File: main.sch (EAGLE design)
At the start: 12 parts

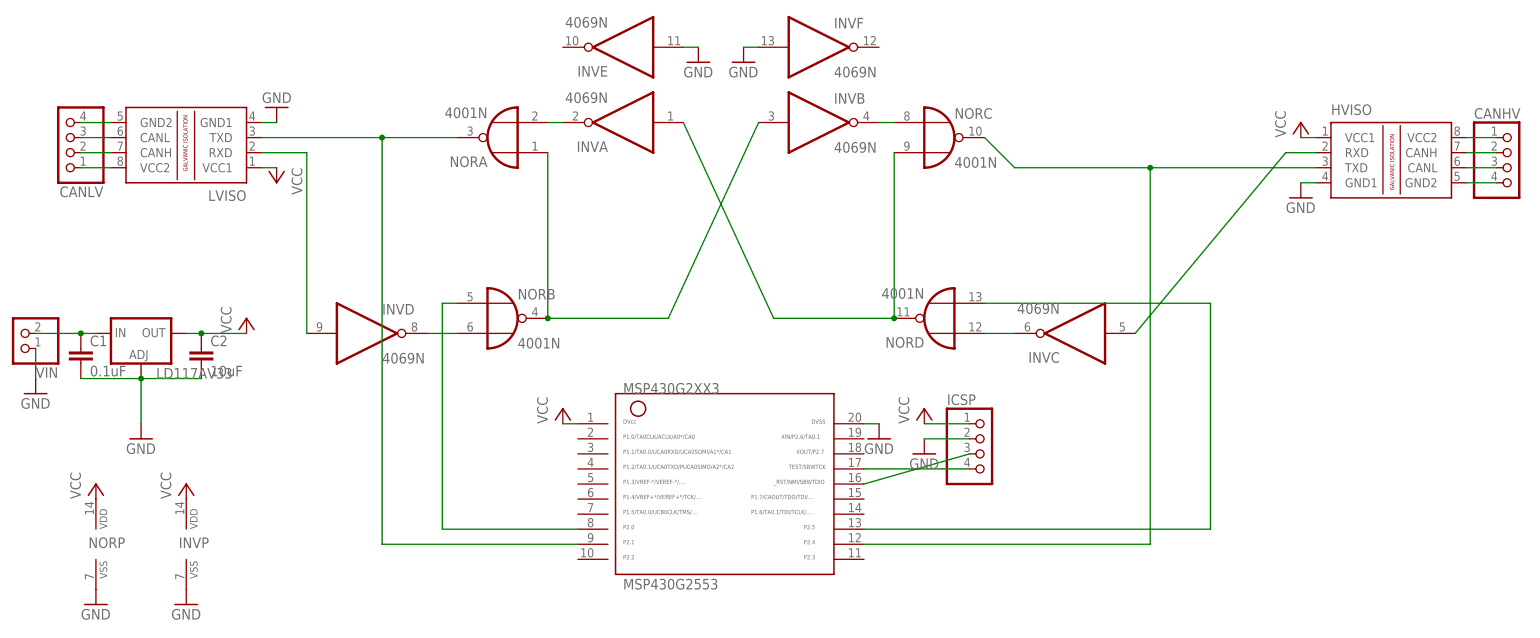
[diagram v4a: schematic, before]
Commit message: Added pin annotations
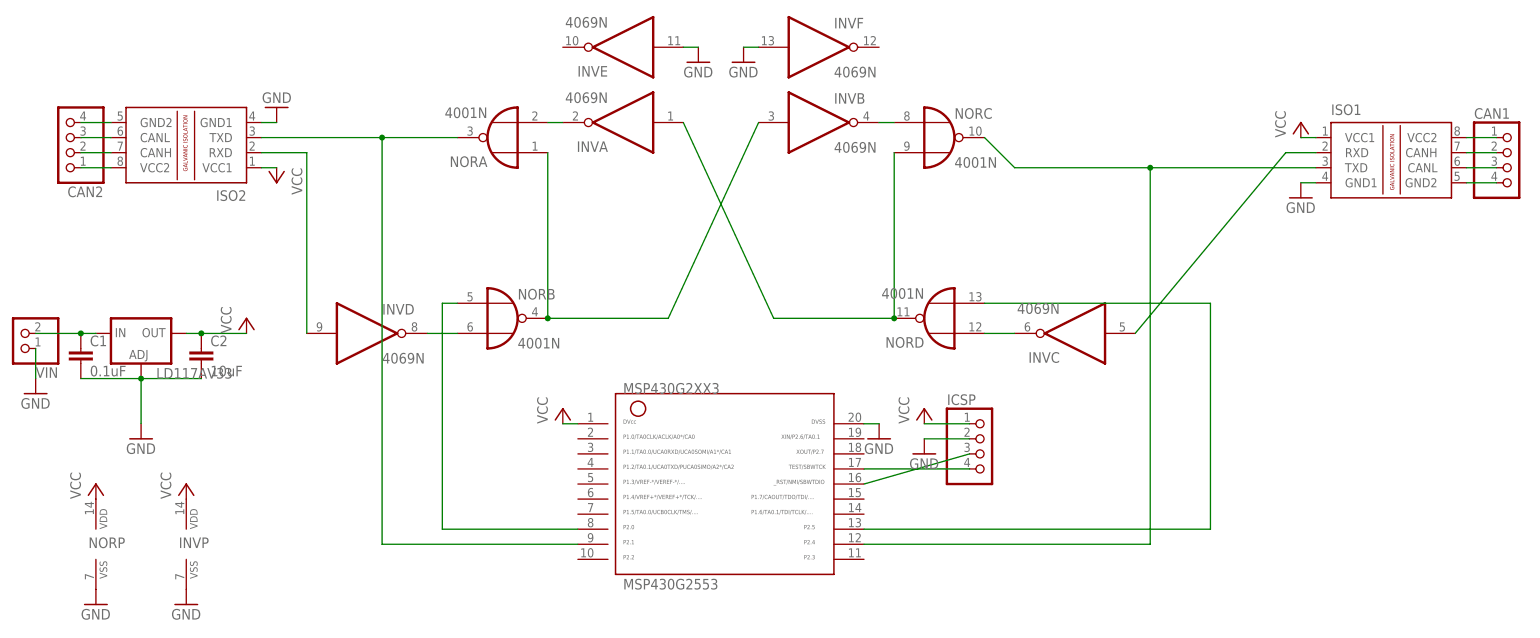
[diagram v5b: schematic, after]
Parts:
- renumbered CANHV to CAN1, CANLV to CAN2, HVISO to ISO1, LVISO to ISO2
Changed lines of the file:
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@@
 <part name="NOR" library="40xx" deviceset="4001" device="N"/>
 <part name="INV" library="40xx" deviceset="4069" device="N"/>
-<part name="HVISO" library="texas" deviceset="ISO1050" device="DUB" value=""/>
-<part name="LVISO" library="texas" deviceset="ISO1050" device="DUB" value=""/>
+<part name="ISO1" library="texas" deviceset="ISO1050" device="DUB" value=""/>
+<part name="ISO2" library="texas" deviceset="ISO1050" device="DUB" value=""/>
 <part name="LD117AV33" library="v-reg" deviceset="LD117A?*" device="V" technology="33" value=""/>
 <part name="P+1" library="supply1" deviceset="VCC" device=""/>
@@
 <part name="P+4" library="supply1" deviceset="VCC" device=""/>
 <part name="GND2" library="supply1" deviceset="GND" device=""/>
-<part name="CANLV" library="pinhead" deviceset="PINHD-1X4" device=""/>
-<part name="CANHV" library="pinhead" deviceset="PINHD-1X4" device=""/>
+<part name="CAN2" library="pinhead" deviceset="PINHD-1X4" device=""/>
+<part name="CAN1" library="pinhead" deviceset="PINHD-1X4" device=""/>
 <part name="GND6" library="supply1" deviceset="GND" device=""/>
 <part name="GND7" library="supply1" deviceset="GND" device=""/>
@@
 <instance part="INV" gate="C" x="182.88" y="53.34" rot="R180"/>
 <instance part="INV" gate="D" x="63.5" y="53.34"/>
-<instance part="HVISO" gate="G$1" x="236.22" y="83.82"/>
-<instance part="LVISO" gate="G$1" x="33.02" y="83.82" rot="R180"/>
+<instance part="ISO1" gate="G$1" x="236.22" y="83.82"/>
+<instance part="ISO2" gate="G$1" x="33.02" y="83.82" rot="R180"/>
 <instance part="LD117AV33" gate="G$1" x="25.4" y="53.34"/>
 <instance part="P+1" gate="VCC" x="43.18" y="55.88"/>
@@
 <instance part="P+4" gate="VCC" x="220.98" y="88.9"/>
 <instance part="GND2" gate="1" x="220.98" y="76.2"/>
-<instance part="CANLV" gate="A" x="12.7" y="86.36" rot="R180"/>
-<instance part="CANHV" gate="A" x="256.54" y="81.28"/>
+<instance part="CAN2" gate="A" x="12.7" y="86.36" rot="R180"/>
+<instance part="CAN1" gate="A" x="256.54" y="81.28"/>
 <instance part="GND6" gate="1" x="17.78" y="7.62"/>
 <instance part="GND7" gate="1" x="33.02" y="7.62"/>
@@
 </segment>
 <segment>
-<pinref part="HVISO" gate="G$1" pin="VCC1"/>
+<pinref part="ISO1" gate="G$1" pin="VCC1"/>
 <pinref part="P+4" gate="VCC" pin="VCC"/>
 <wire x1="220.98" y1="86.36" x2="223.52" y2="86.36" width="0.1524" layer="91"/>
 </segment>
 <segment>
-<pinref part="LVISO" gate="G$1" pin="VCC1"/>
+<pinref part="ISO2" gate="G$1" pin="VCC1"/>
 <wire x1="48.26" y1="81.28" x2="45.72" y2="81.28" width="0.1524" layer="91"/>
 <pinref part="P+5" gate="VCC" pin="VCC"/>
@@
 </segment>
 <segment>
-<pinref part="HVISO" gate="G$1" pin="GND1"/>
+<pinref part="ISO1" gate="G$1" pin="GND1"/>
 <pinref part="GND2" gate="1" pin="GND"/>
 <wire x1="220.98" y1="78.74" x2="223.52" y2="78.74" width="0.1524" layer="91"/>
@@
 </segment>
 <segment>
-<pinref part="LVISO" gate="G$1" pin="GND1"/>
+<pinref part="ISO2" gate="G$1" pin="GND1"/>
 <wire x1="48.26" y1="88.9" x2="45.72" y2="88.9" width="0.1524" layer="91"/>
 <pinref part="GND3" gate="1" pin="GND"/>
@@
 <net name="N$13" class="0">
 <segment>
-<pinref part="HVISO" gate="G$1" pin="VCC2"/>
-<pinref part="CANHV" gate="A" pin="1"/>
+<pinref part="ISO1" gate="G$1" pin="VCC2"/>
+<pinref part="CAN1" gate="A" pin="1"/>
 <wire x1="254" y1="86.36" x2="248.92" y2="86.36" width="0.1524" layer="91"/>
 </segment>
@@
 <net name="N$14" class="0">
 <segment>
-<pinref part="HVISO" gate="G$1" pin="CANH"/>
-<pinref part="CANHV" gate="A" pin="2"/>
+<pinref part="ISO1" gate="G$1" pin="CANH"/>
+<pinref part="CAN1" gate="A" pin="2"/>
 <wire x1="254" y1="83.82" x2="248.92" y2="83.82" width="0.1524" layer="91"/>
 </segment>
@@
 <net name="N$15" class="0">
 <segment>
-<pinref part="HVISO" gate="G$1" pin="CANL"/>
-<pinref part="CANHV" gate="A" pin="3"/>
+<pinref part="ISO1" gate="G$1" pin="CANL"/>
+<pinref part="CAN1" gate="A" pin="3"/>
 <wire x1="254" y1="81.28" x2="248.92" y2="81.28" width="0.1524" layer="91"/>
 </segment>
@@
 <net name="N$16" class="0">
 <segment>
-<pinref part="HVISO" gate="G$1" pin="GND2"/>
-<pinref part="CANHV" gate="A" pin="4"/>
+<pinref part="ISO1" gate="G$1" pin="GND2"/>
+<pinref part="CAN1" gate="A" pin="4"/>
 <wire x1="254" y1="78.74" x2="248.92" y2="78.74" width="0.1524" layer="91"/>
 </segment>
@@
 <segment>
 <pinref part="INV" gate="C" pin="I"/>
-<pinref part="HVISO" gate="G$1" pin="RXD"/>
+<pinref part="ISO1" gate="G$1" pin="RXD"/>
 <wire x1="193.04" y1="53.34" x2="218.44" y2="83.82" width="0.1524" layer="91"/>
 <wire x1="218.44" y1="83.82" x2="223.52" y2="83.82" width="0.1524" layer="91"/>
@@
 <segment>
 <pinref part="NOR" gate="C" pin="O"/>
-<pinref part="HVISO" gate="G$1" pin="TXD"/>
+<pinref part="ISO1" gate="G$1" pin="TXD"/>
 <wire x1="167.64" y1="86.36" x2="172.72" y2="81.28" width="0.1524" layer="91"/>
 <wire x1="172.72" y1="81.28" x2="195.58" y2="81.28" width="0.1524" layer="91"/>
@@
 <segment>
 <pinref part="NOR" gate="A" pin="O"/>
-<pinref part="LVISO" gate="G$1" pin="TXD"/>
+<pinref part="ISO2" gate="G$1" pin="TXD"/>
 <wire x1="78.74" y1="86.36" x2="66.04" y2="86.36" width="0.1524" layer="91"/>
 <wire x1="66.04" y1="86.36" x2="45.72" y2="86.36" width="0.1524" layer="91"/>
@@
 <net name="N$20" class="0">
 <segment>
-<pinref part="LVISO" gate="G$1" pin="RXD"/>
+<pinref part="ISO2" gate="G$1" pin="RXD"/>
 <pinref part="INV" gate="D" pin="I"/>
 <wire x1="45.72" y1="83.82" x2="53.34" y2="83.82" width="0.1524" layer="91"/>
@@
 <net name="N$9" class="0">
 <segment>
-<pinref part="CANLV" gate="A" pin="1"/>
-<pinref part="LVISO" gate="G$1" pin="VCC2"/>
+<pinref part="CAN2" gate="A" pin="1"/>
+<pinref part="ISO2" gate="G$1" pin="VCC2"/>
 <wire x1="15.24" y1="81.28" x2="20.32" y2="81.28" width="0.1524" layer="91"/>
 </segment>
@@
 <net name="N$10" class="0">
 <segment>
-<pinref part="CANLV" gate="A" pin="2"/>
-<pinref part="LVISO" gate="G$1" pin="CANH"/>
+<pinref part="CAN2" gate="A" pin="2"/>
+<pinref part="ISO2" gate="G$1" pin="CANH"/>
 <wire x1="15.24" y1="83.82" x2="20.32" y2="83.82" width="0.1524" layer="91"/>
 </segment>
@@
 <net name="N$11" class="0">
 <segment>
-<pinref part="CANLV" gate="A" pin="3"/>
-<pinref part="LVISO" gate="G$1" pin="CANL"/>
+<pinref part="CAN2" gate="A" pin="3"/>
+<pinref part="ISO2" gate="G$1" pin="CANL"/>
 <wire x1="15.24" y1="86.36" x2="20.32" y2="86.36" width="0.1524" layer="91"/>
 </segment>
@@
 <net name="N$12" class="0">
 <segment>
-<pinref part="CANLV" gate="A" pin="4"/>
-<pinref part="LVISO" gate="G$1" pin="GND2"/>
+<pinref part="CAN2" gate="A" pin="4"/>
+<pinref part="ISO2" gate="G$1" pin="GND2"/>
 <wire x1="15.24" y1="88.9" x2="20.32" y2="88.9" width="0.1524" layer="91"/>
 </segment>
